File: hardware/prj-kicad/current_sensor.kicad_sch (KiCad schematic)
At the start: 12 parts

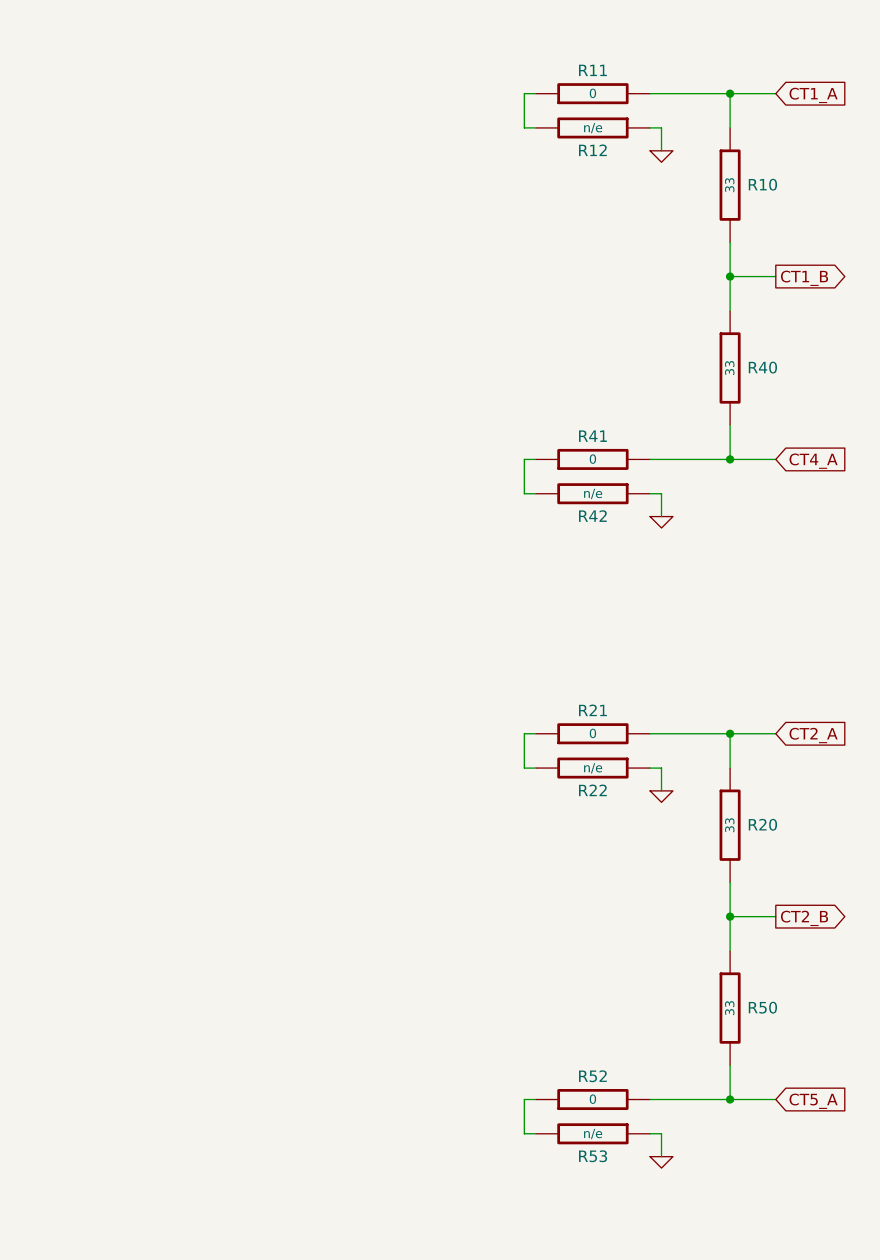
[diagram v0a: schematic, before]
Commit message: Hardware: Add power supply
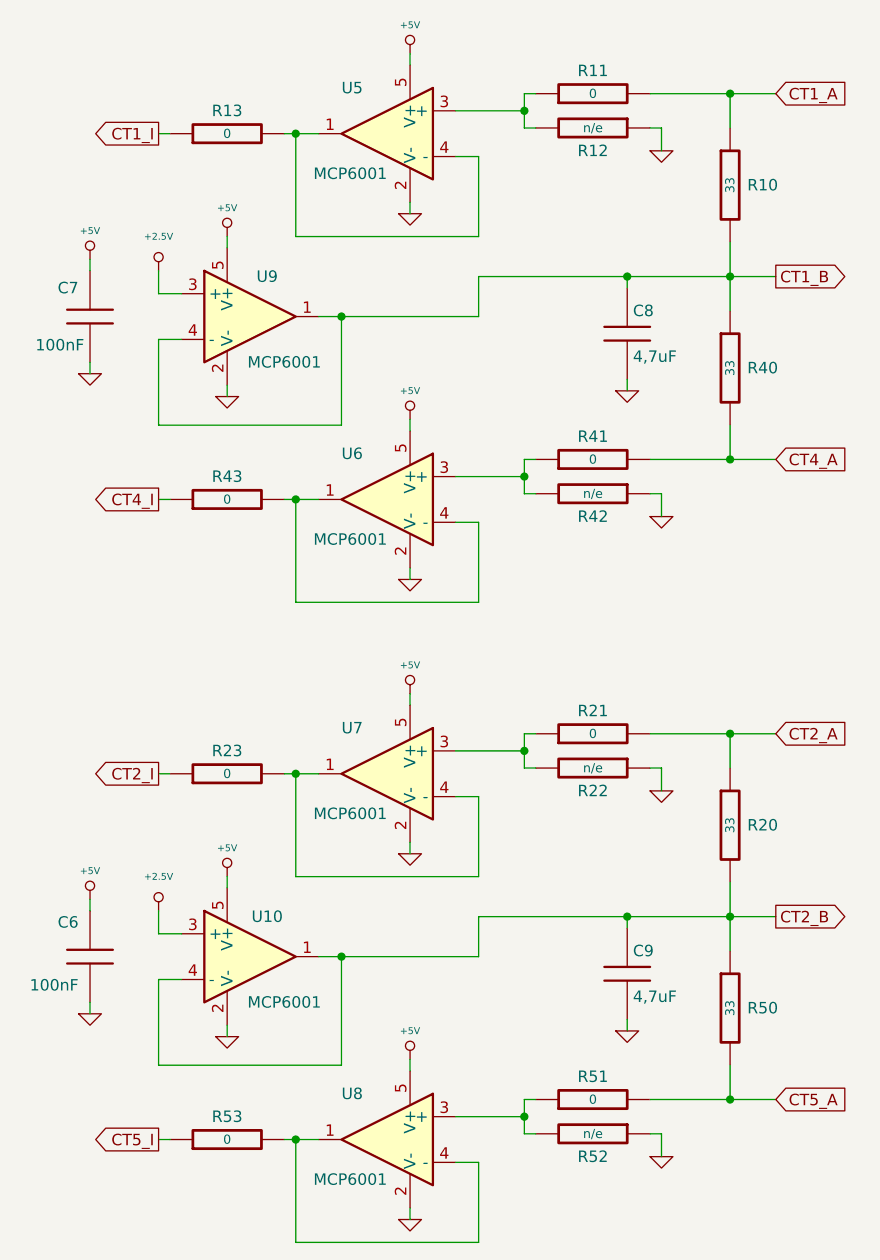
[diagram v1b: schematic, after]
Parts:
- added C6, C7: 100nF, cowdin-3a-pwrmon:SMD0603, symbol cowdin-3a-pwrmon:C
- added C8, C9: 4,7uF, cowdin-3a-pwrmon:SMD0805, symbol cowdin-3a-pwrmon:C
- added R13, R23, R43, R53: 0, cowdin-3a-pwrmon:SMD0603, symbol cowdin-3a-pwrmon:R
- added U10, U5, U6, U7, U8, U9: MCP6001, cowdin-3a-pwrmon:SOT23-5, symbol cowdin-3a-pwrmon:MCP6001
- renumbered R52 to R51, R53 to R52
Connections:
- net CT1_B: now also C8.1, U9.1, U9.4 (-)
- net CT2_B: now also C9.1, U10.1, U10.4 (-)
- net GND: now also C6.2, C7.2, C8.2, C9.2, U10.2 (V-), U5.2 (V-), U6.2 (V-), U7.2 (V-), U8.2 (V-), U9.2 (V-)
- net at R21.1, R22.2: now also U7.3 (+)
- net at R51.1, R52.2: now also U8.3 (+)
- net at R41.1, R42.2: now also U6.3 (+)
- net at R11.1, R12.2: now also U5.3 (+)
- new net: R53.2, U8.1, U8.4 (-)
- new net: R43.2, U6.1, U6.4 (-)
- new net: R13.2, U5.1, U5.4 (-)
- new net: R23.2, U7.1, U7.4 (-)
- new net +2.5V: U10.3 (+), U9.3 (+)
- new net +5V: C6.1, C7.1, U10.5 (V+), U5.5 (V+), U6.5 (V+), U7.5 (V+), U8.5 (V+), U9.5 (V+)
- new net CT1_I: R13.1
- new net CT2_I: R23.1
- new net CT4_I: R43.1
- new net CT5_I: R53.1

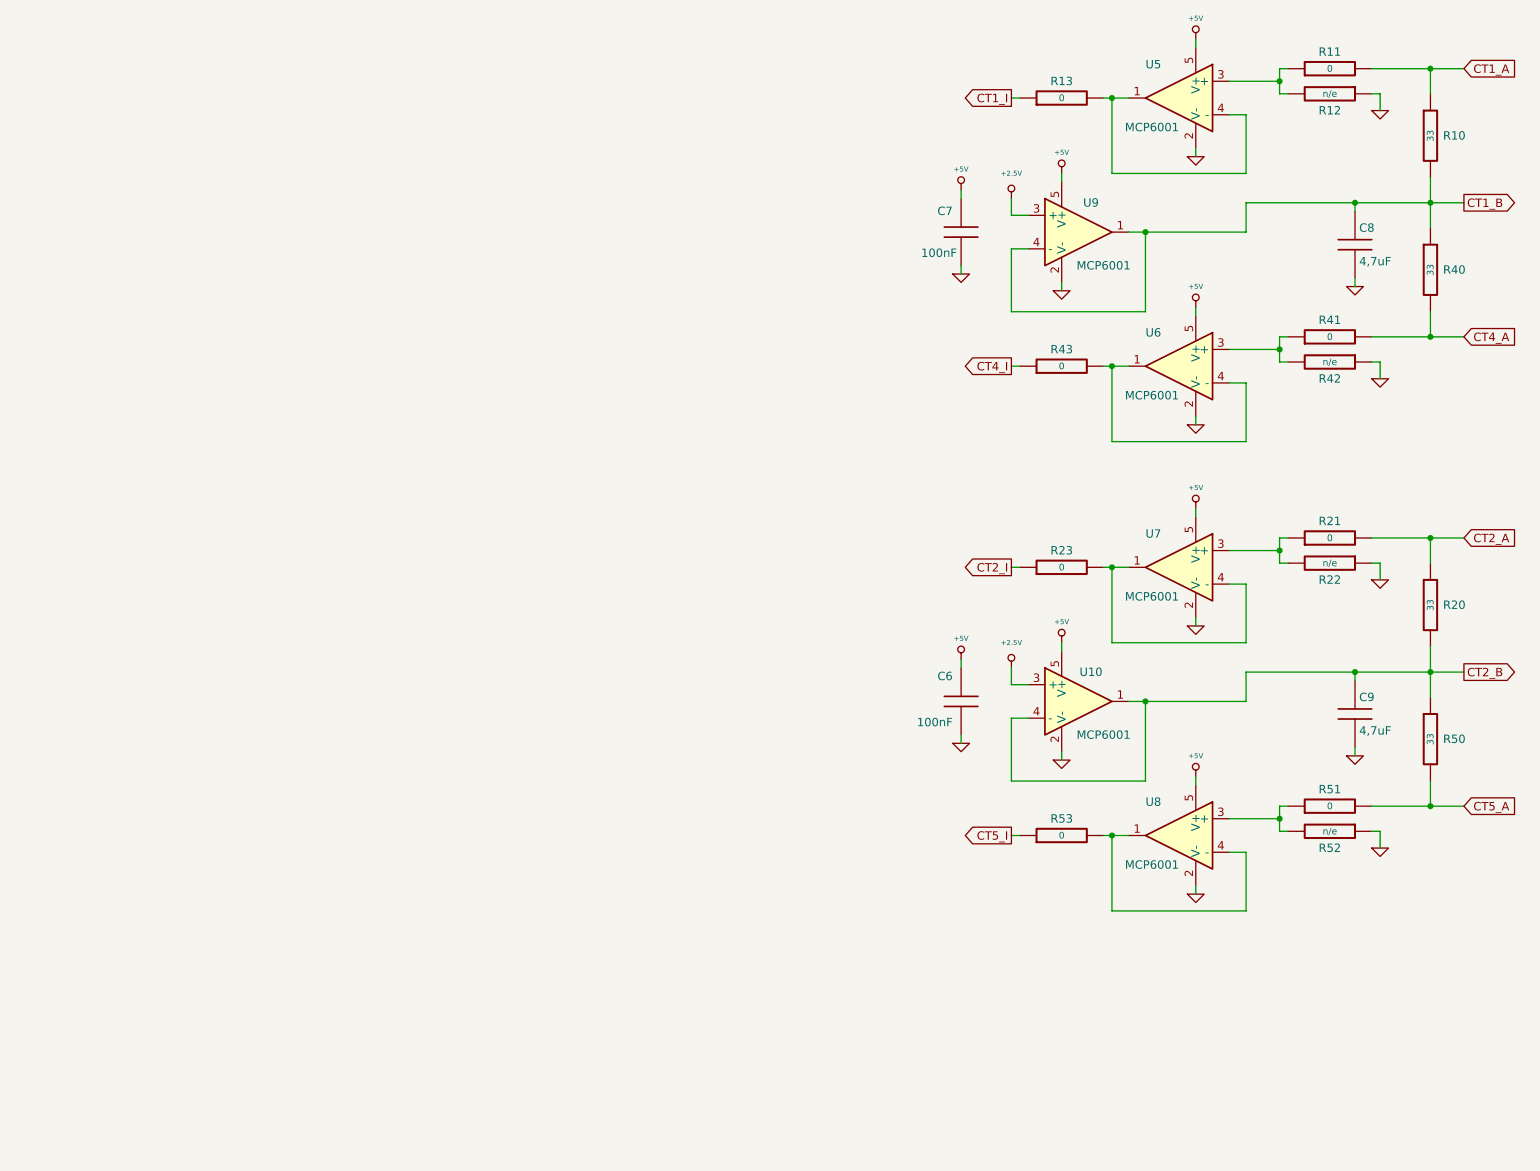
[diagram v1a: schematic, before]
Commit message: Hardware: Finish current sensor interface and create production files for rev1
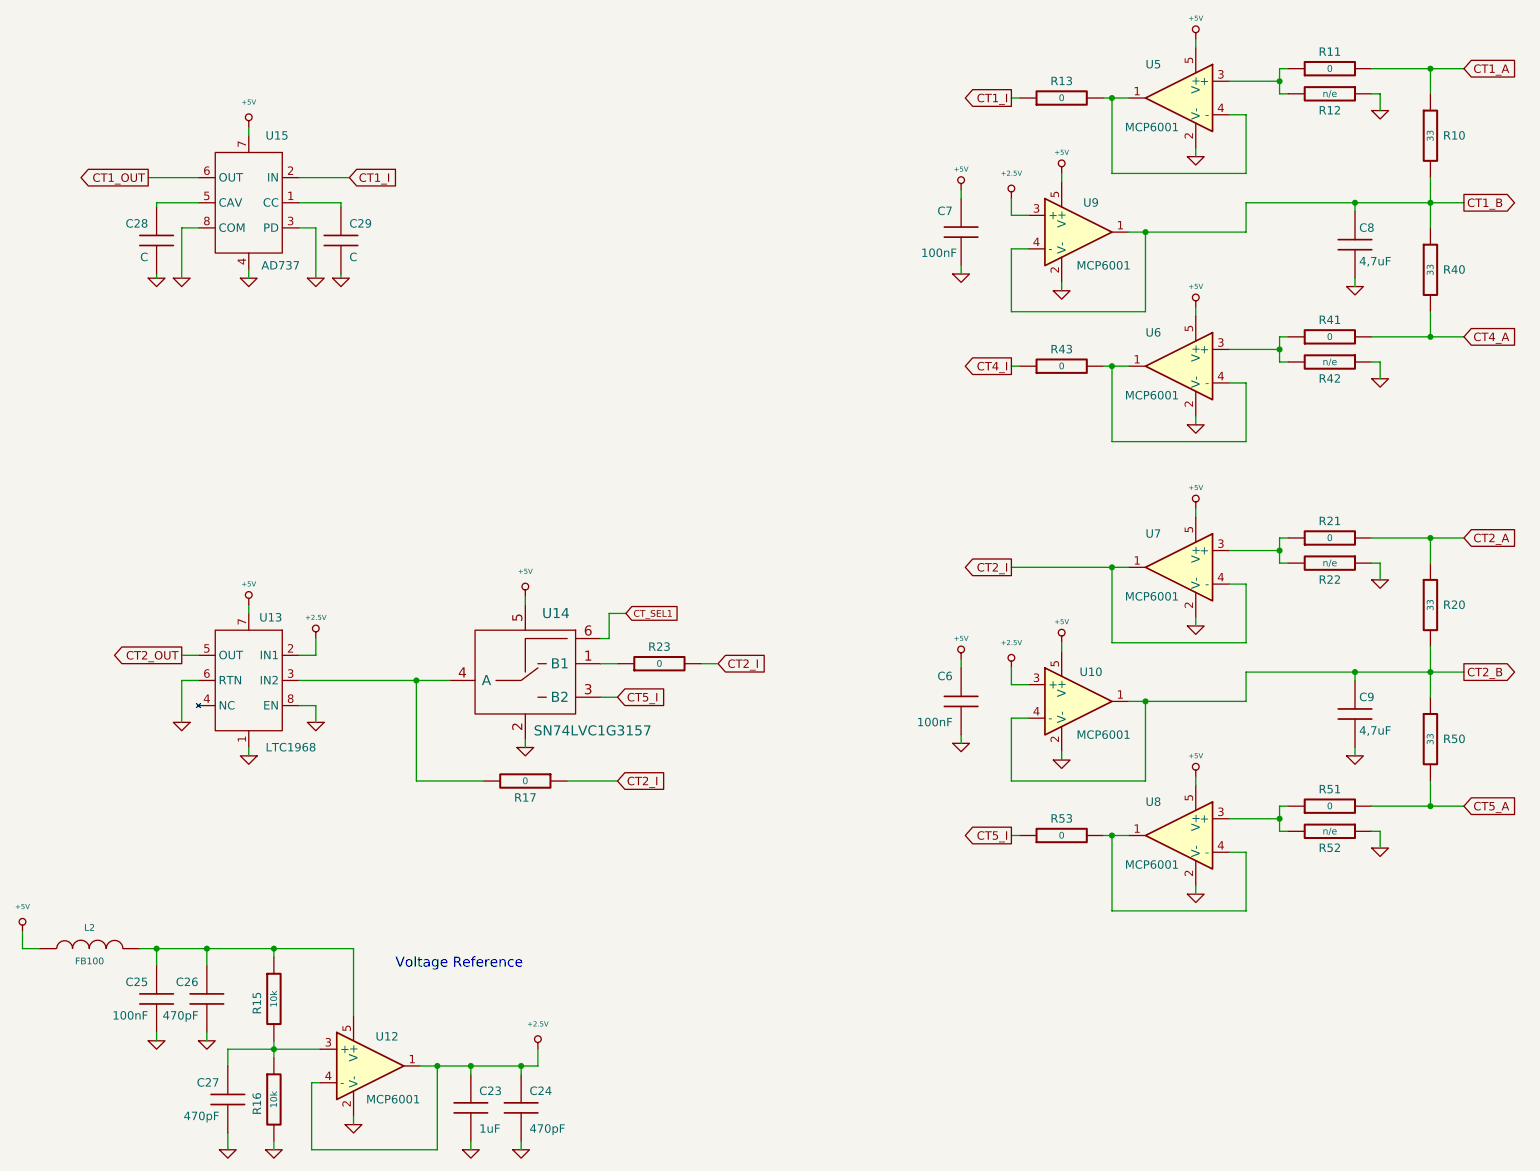
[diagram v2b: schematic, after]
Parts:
- added C23: 1uF, cowdin-3a-pwrmon:SMD0603, symbol cowdin-3a-pwrmon:C
- added C24, C26, C27: 470pF, cowdin-3a-pwrmon:SMD0603, symbol cowdin-3a-pwrmon:C
- added C25: 100nF, cowdin-3a-pwrmon:SMD0603, symbol cowdin-3a-pwrmon:C
- added C28, C29: C, cowdin-3a-pwrmon:SMD0603, symbol cowdin-3a-pwrmon:C
- added L2: FB100, cowdin-3a-pwrmon:SMD0603, symbol cowdin-3a-pwrmon:INDUCTOR
- added R15, R16: 10k, cowdin-3a-pwrmon:SMD0603, symbol cowdin-3a-pwrmon:R
- added R17: 0, cowdin-3a-pwrmon:SMD0603, symbol cowdin-3a-pwrmon:R
- added U12: MCP6001, cowdin-3a-pwrmon:SOT23-5, symbol cowdin-3a-pwrmon:MCP6001
- added U13: LTC1968, cowdin-3a-pwrmon:MSOP-8, symbol cowdin-3a-pwrmon:LTC1968
- added U14: SN74LVC1G3157, cowdin-3a-pwrmon:SC70-6, symbol cowdin-3a-pwrmon:SN74LVC1G3157
- added U15: AD737, cowdin-3a-pwrmon:SOIC-8E, symbol cowdin-3a-pwrmon:AD737
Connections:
- net +2.5V: now also C23.1, C24.1, U12.1, U12.4 (-), U13.2 (IN1)
- net +5V: now also L2.1, U13.7, U14.5, U15.7
- net CT1_I: now also U15.2 (IN)
- net CT2_I: now also R23.2, U7.1, U7.4 (-), R17.1; no longer R23.1
- net CT5_I: now also U14.3 (B2)
- net GND: now also C23.2, C24.2, C25.2, C26.2, C27.2, C28.2, C29.2, R16.2, U12.2 (V-), U13.1, U13.6 (RTN), U13.8 (EN), U14.2, U15.3 (PD), U15.4, U15.8 (COM)
- new net: C29.1, U15.1 (CC)
- new net: C28.1, U15.5 (CAV)
- new net: C25.1, C26.1, L2.2, R15.1, U12.5 (V+)
- new net: R17.2, U13.3 (IN2), U14.4 (A)
- new net: C27.1, R15.2, R16.1, U12.3 (+)
- new net: R23.1, U14.1 (B1)
- new net CT1_OUT: U15.6 (OUT)
- new net CT2_OUT: U13.5 (OUT)
- new net CT_SEL1: U14.6
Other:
- note added: "Voltage Reference"
- moved on the sheet: R23
